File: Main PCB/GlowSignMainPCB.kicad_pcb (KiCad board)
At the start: 2 copper layers, 169.5 x 83.5 mm, 132 parts, among them P1 Solder_Pad, P2 Solder_Pad, P3 Solder_Pad, P4 Solder_Pad, P5 Solder_Pad, P6 Solder_Pad, P7 Solder_Pad, SW1 TS-1185EC-C-D-B, SW2 TS-1185EC-C-D-B, SW3 TS24CA, U12 AO3400A, U13 AP40P05, U14 AP40P05, U16 AP40P05, U17 SS54, U18 BL1117-33CX, U19 TPS3839G33DBZR, U2 SS54, U20 MSM261D4030H1CPM, U3 SN74LVC2T45DCUR, U4 ESP32-WROOM-32E, U7 CP2102-GMR, U8 UMH3N

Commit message: updated pcb designs
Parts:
- removed C56: 220uF, Capacitor_SMD:C_1206_3216Metric_Pad1.33x1.80mm_HandSolder
- removed JP1, JP2: SolderJumper_2_Open, Jumper:SolderJumper-2_P1.3mm_Open_RoundedPad1.0x1.5mm
- removed R21: 10K, Resistor_SMD:R_0603_1608Metric_Pad0.98x0.95mm_HandSolder
- removed U16: AP40P05, footprint:SOT-23-3_L2.9-W1.3-P1.90-LS2.4-BR
- removed U17: SS54, footprint:SMA_L4.4-W2.8-LS5.4-RD
- R11: value 100K -> 160K
- moved R20 20.4 mm to (213.1, 111.7)
- moved U14 20.4 mm to (213.1, 114.4)
- moved C3 5.68 mm to (219.3, 133.9)
- moved C55 5.67 mm to (215.7, 133.9)
- moved U13 4.23 mm to (217.5, 130.6)
- moved R18 4.23 mm to (217.5, 127.9)
- moved U2 3.26 mm to (169.0, 132.0)
- turned R4 to 0 degrees
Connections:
- C2 pad 1: +3V3 -> 3.3V AFTER RELAY
- C3 pad 1: +5V -> LED 5V
- C54 pad 1: +5V -> LED 5V
- C55 pad 1: +5V -> LED 5V
- JP3 pad 1: +3V3 -> 3.3V AFTER RELAY
- R20 pad 2: +5V -> +3V3
- TP2 pad 1: IO18/MAINBUTTON -> IO33/MAINBUTTON
- TP6 pad 1: +3V3 -> 3.3V AFTER RELAY
- U14 pad 2: +5V -> +3V3
- U14 pad 3: LED 5V -> 3.3V AFTER RELAY
- U3 pad 1: +5V -> LED 5V
- U3 pad 8: +3V3 -> 3.3V AFTER RELAY
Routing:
- net 3.3V AFTER RELAY: track 0.00 -> 70.5 mm, vias 0 -> 3
- net +3V3: track 140.0 -> 101.8 mm, vias 12 -> 11
- net +5V: track 144.8 -> 113.3 mm
- net LED 5V: track 641.1 -> 658.7 mm, vias 68 -> 70
- net GND: track 941.1 -> 929.0 mm, vias 112 -> 117
- net Net-(R18-Pad1): track 25.0 -> 20.6 mm, vias 4 -> 2
- net Net-(R4-Pad1): track 42.1 -> 46.2 mm
- net VBUS: track 180.6 -> 177.2 mm
- net IO33/MAINBUTTON: track 83.9 -> 85.8 mm
- net USB-C DATA+: track 93.2 -> 91.9 mm
- net USB-C DATA-: track 98.7 -> 97.8 mm
- net +BATT: track 162.4 -> 163.3 mm
- net IO14/SCK: track 23.5 -> 22.6 mm
- net EN: track 37.8 -> 37.0 mm
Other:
- board text removed: "LEDs always on"

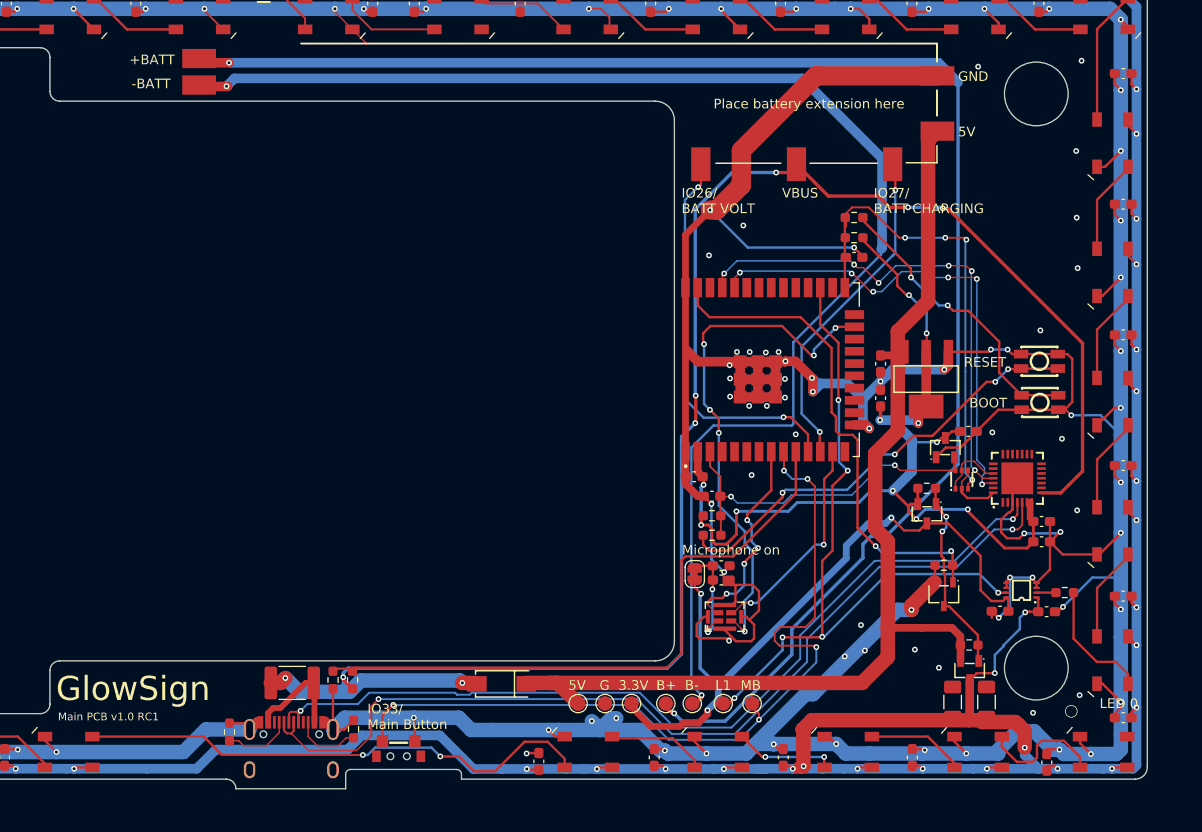
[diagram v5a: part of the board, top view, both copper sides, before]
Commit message: fixed deep sleep power consumption + new LED0
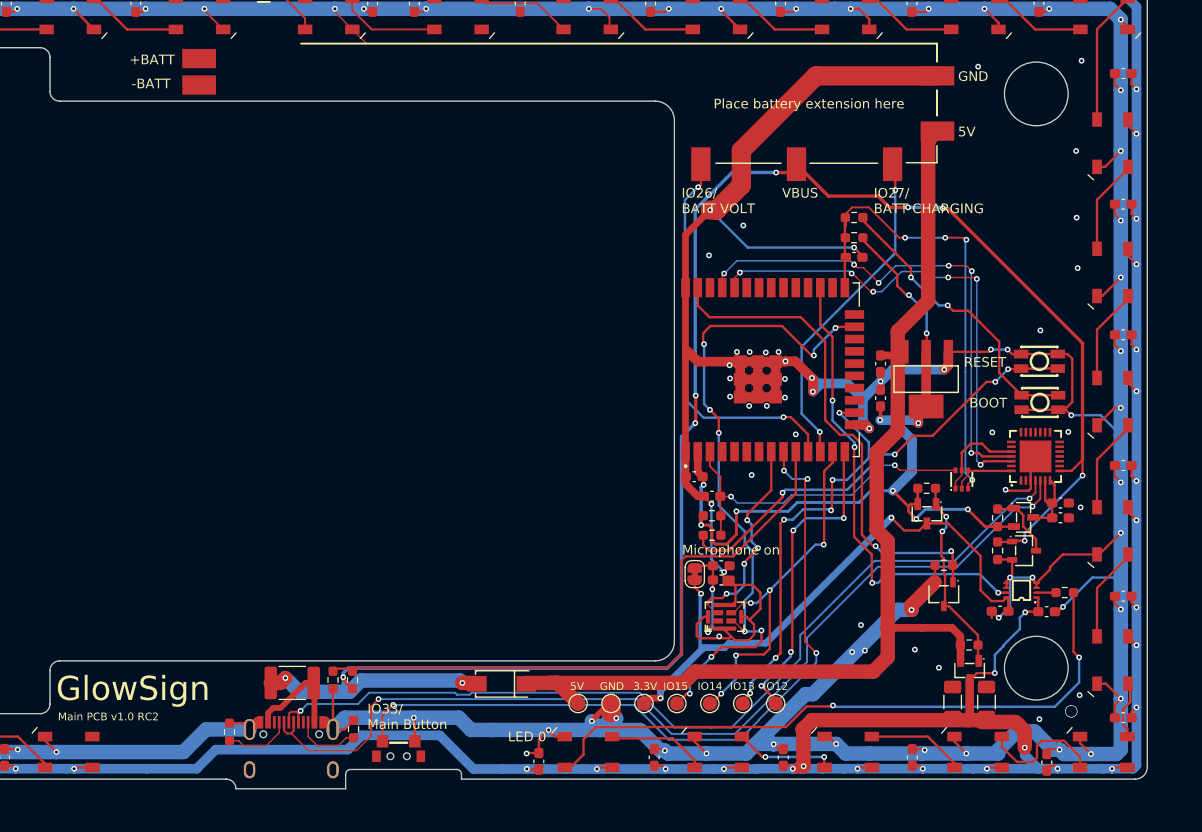
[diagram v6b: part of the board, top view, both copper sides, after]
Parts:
- removed C57: 0.1uF, Capacitor_SMD:C_0603_1608Metric_Pad1.08x0.95mm_HandSolder
- removed U19: TPS3839G33DBZR, footprint:SOT-23-3_L2.9-W1.3-P1.90-LS2.4-BR
- added R8: 10K, Resistor_SMD:R_0603_1608Metric_Pad0.98x0.95mm_HandSolder, F.Cu at (220.4, 114.8)
- added R9: 10K, Resistor_SMD:R_0603_1608Metric_Pad0.98x0.95mm_HandSolder, F.Cu at (220.4, 118.2)
- added U1: AP40P05, footprint:SOT-23-3_L2.9-W1.3-P1.90-LS2.4-BR, F.Cu at (223.1, 114.7)
- added U5: AO3400A, footprint:SOT-23-3_L2.9-W1.6-P1.90-LS2.8-BR, F.Cu at (223.1, 118.2)
- C8: value 1uF -> 10uF
- moved TP1 5.44 mm to (197.4, 134.0)
- moved TP4 4.56 mm to (190.6, 134.0)
- moved C4 3.16 mm to (226.9, 114.8)
- moved U7 2.94 mm to (224.3, 108.4)
- moved C6 2.74 mm to (226.9, 113.2)
- moved TP5 1.59 mm to (187.2, 134.0)
- moved TP6 1.29 mm to (183.8, 134.0)
- moved TP2 0.97 mm to (194.0, 134.0)
- moved TP7 0.62 mm to (180.3, 134.0)
- turned C8 to 0 degrees
- renumbered C46 to C18, C47 to C19, C48 to C20, C49 to C21, C50 to C22, C18 to C23, C19 to C24, C20 to C25, C21 to C26, C22 to C27, C23 to C28, C24 to C29, C25 to C30, C26 to C31, C27 to C32, C28 to C33, C29 to C34, C30 to C35, C31 to C36, C32 to C37, C33 to C38, C34 to C39, C35 to C40, C36 to C41, C37 to C42, C38 to C43, C39 to C44, C40 to C45, C41 to C46, C42 to C47, C43 to C48, C44 to C49, C45 to C50, D5 to D10, D6 to D11, D7 to D12, D8 to D13, D9 to D14, D10 to D15, D11 to D16, D12 to D17, D13 to D18, D14 to D19, D15 to D20, D16 to D21, D17 to D22, D18 to D23, D19 to D24, D20 to D25, D21 to D26, D22 to D27, D23 to D28, D24 to D29, D31 to D3, D25 to D30, D26 to D31, D27 to D32, D28 to D33, D29 to D34, D30 to D35, D32 to D4, D33 to D5, D34 to D6, D35 to D7, D3 to D8, D4 to D9
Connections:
- net 3.3V AFTER RELAY renamed 3.3V AFTER MOSFET
- net IO23/LEDPOWER renamed IO23/POWERMOSFETS
- net LED 5V renamed 5V AFTER MOSFET
- C4 pad 2: +3V3 -> Net-(C4-Pad2)
- C6 pad 1: +3V3 -> Net-(C4-Pad2)
- C8 pad 1: EN -> GND
- C8 pad 2: GND -> EN
- D3 pad 4: Net-(D30-Pad2) (its old number) -> LED1 DATA OUT
- D35 pad 2: Net-(D30-Pad2) (its old number) -> unconnected-(D35-Pad2)
- D7 pad 2: unconnected-(D35-Pad2) -> Net-(D7-Pad2)
- D8 pad 4: LED1 DATA OUT -> Net-(D7-Pad2)
- TP1 pad 1: IO16/LED1 -> IO12/TDI
- TP2 pad 1: IO33/MAINBUTTON -> IO13/TCK
- TP4 pad 1: +BATT -> IO14/SCK/TMS
- TP5 pad 1: -BATT -> IO15/WS/TDO
- U20 pad 2: IO15/WS -> IO15/WS/TDO
- U20 pad 3: IO14/SCK -> IO14/SCK/TMS
- U4 pad 13: IO14/SCK -> IO14/SCK/TMS
- U4 pad 14: unconnected-(U4-Pad14) -> IO12/TDI
- U4 pad 16: unconnected-(U4-Pad16) -> IO13/TCK
- U4 pad 23: IO15/WS -> IO15/WS/TDO
- U7 pad 6: +3V3 -> Net-(C4-Pad2)
- U7 pad 7: +3V3 -> Net-(C4-Pad2)
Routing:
- net +BATT: track 163.3 -> 0.00 mm, vias 2 -> 0
- net -BATT: track 145.4 -> 0.00 mm, vias 2 -> 0
- net IO15/WS/TDO: track 0.00 -> 69.3 mm, vias 0 -> 9
- net LED1 DATA OUT: track 12.9 -> 68.2 mm, vias 0 -> 2
- net Net-(D30-Pad2) (its old number): track 54.4 -> 0.00 mm, vias 2 -> 0
- net IO15/WS: track 54.1 -> 0.00 mm, vias 6 -> 0
- net IO13/TCK: track 0.00 -> 41.6 mm, vias 0 -> 6
- net IO14/SCK/TMS: track 0.00 -> 38.7 mm, vias 0 -> 5
- net IO12/TDI: track 0.00 -> 32.6 mm, vias 0 -> 4
- net IO16/LED1: track 75.1 -> 48.1 mm, vias 6 -> 4
- net IO14/SCK: track 22.6 -> 0.00 mm, vias 2 -> 0
- net GND: track 929.0 -> 915.6 mm, vias 117 -> 116
- net +3V3: track 101.8 -> 88.6 mm, vias 11 -> 10
- net VBUS: track 177.2 -> 187.4 mm, vias 8 -> 10
- net Net-(C4-Pad2): track 0.00 -> 9.07 mm
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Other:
- board text added: "IO12"
- board text added: "IO13"
- board text added: "IO14"
- board text added: "IO15"
- board text added: "Main PCB v1.0 RC2"
- board text removed: "B+"
- board text removed: "B-"
- board text removed: "G"
- board text removed: "L1"
- board text removed: "MB"
- board text removed: "Main PCB v1.0 RC1"

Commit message: updated case design
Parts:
- added SW4: TS24CA, footprint:SW-SMD_TS24CA, F.Cu at (136.0, 139.8)
- added U6: SN74LVC1G373DBVR, footprint:SOT-23-6_L2.9-W1.6-P0.95-LS2.8-BR, F.Cu at (190.7, 87.4)
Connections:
- R19 pad 2: IO23/POWERMOSFETS -> Net-(R19-Pad2)
- SW3 pad 3: GND -> +3V3
- U12 pad 1: IO23/POWERMOSFETS -> Net-(R19-Pad2)
- U4 pad 26: unconnected-(U4-Pad26) -> IO4/BUTTON 2
- U4 pad 31: IO19 -> unconnected-(U4-Pad31)
- U4 pad 36: unconnected-(U4-Pad36) -> IO22/LED LETCH EN
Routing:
- net IO4/BUTTON 2: track 0.00 -> 259.4 mm, vias 0 -> 4
- net Net-(R19-Pad2): track 0.00 -> 55.7 mm, vias 0 -> 4
- net IO23/POWERMOSFETS: track 52.4 -> 2.62 mm, vias 2 -> 0
- net +3V3: track 88.6 -> 107.0 mm, vias 10 -> 12
- net IO22/LED LETCH EN: track 0.00 -> 5.40 mm
- net 5V AFTER MOSFET: track 657.8 -> 659.1 mm
- net GND: track 915.6 -> 915.3 mm, vias 116 -> 117
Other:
- board text added: "IO33"
- board text added: "IO4"
- board text added: "Main PCB v1.0 RC3"
- board text removed: "IO33/ Main Button"
- board text removed: "Main PCB v1.0 RC2"
